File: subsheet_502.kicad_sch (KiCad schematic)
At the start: 26 parts, among them U500 74F374_OCTAL_D-TYPE_EDGE-TRIG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, U501 74F374_OCTAL_D-TYPE_EDGE-TRIG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, U502 DAC0802LCN_PHY, U503 DAC0802LCN_PHY

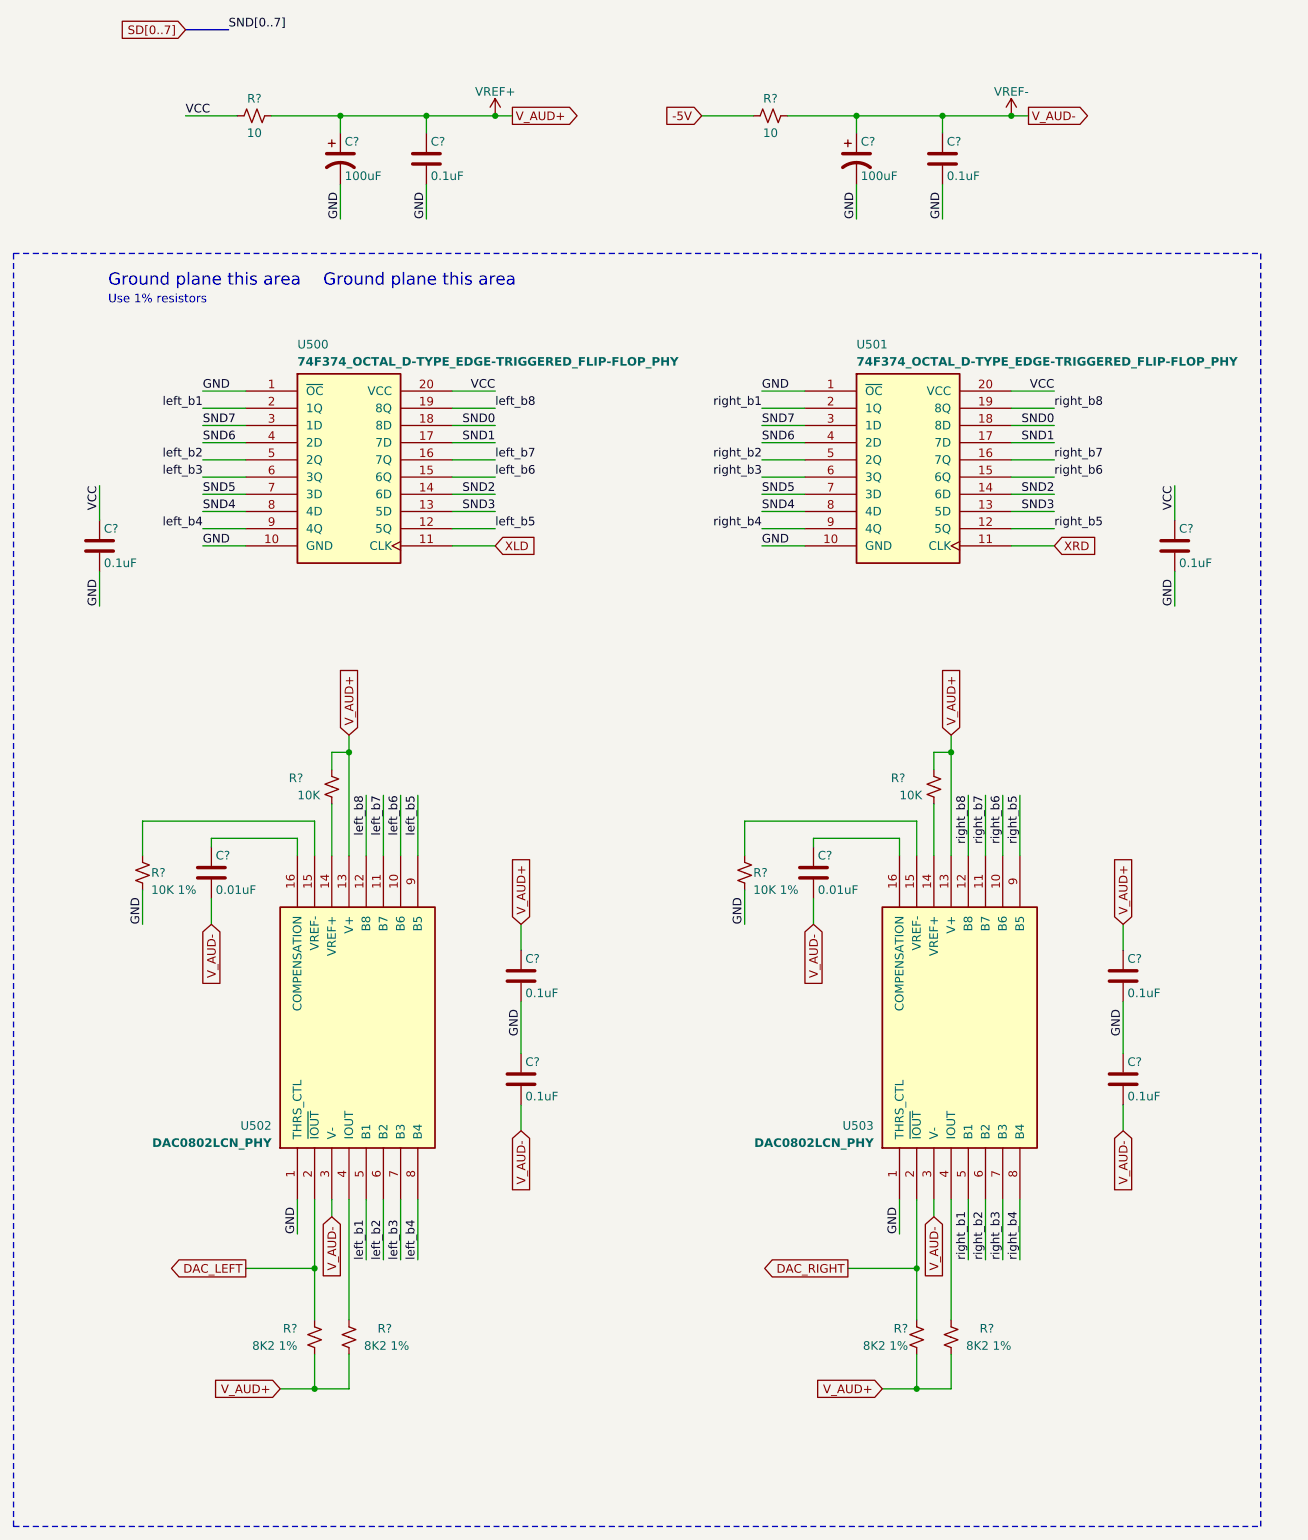
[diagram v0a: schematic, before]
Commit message: Resolves #3 : [schematic] annotate video port with signal name
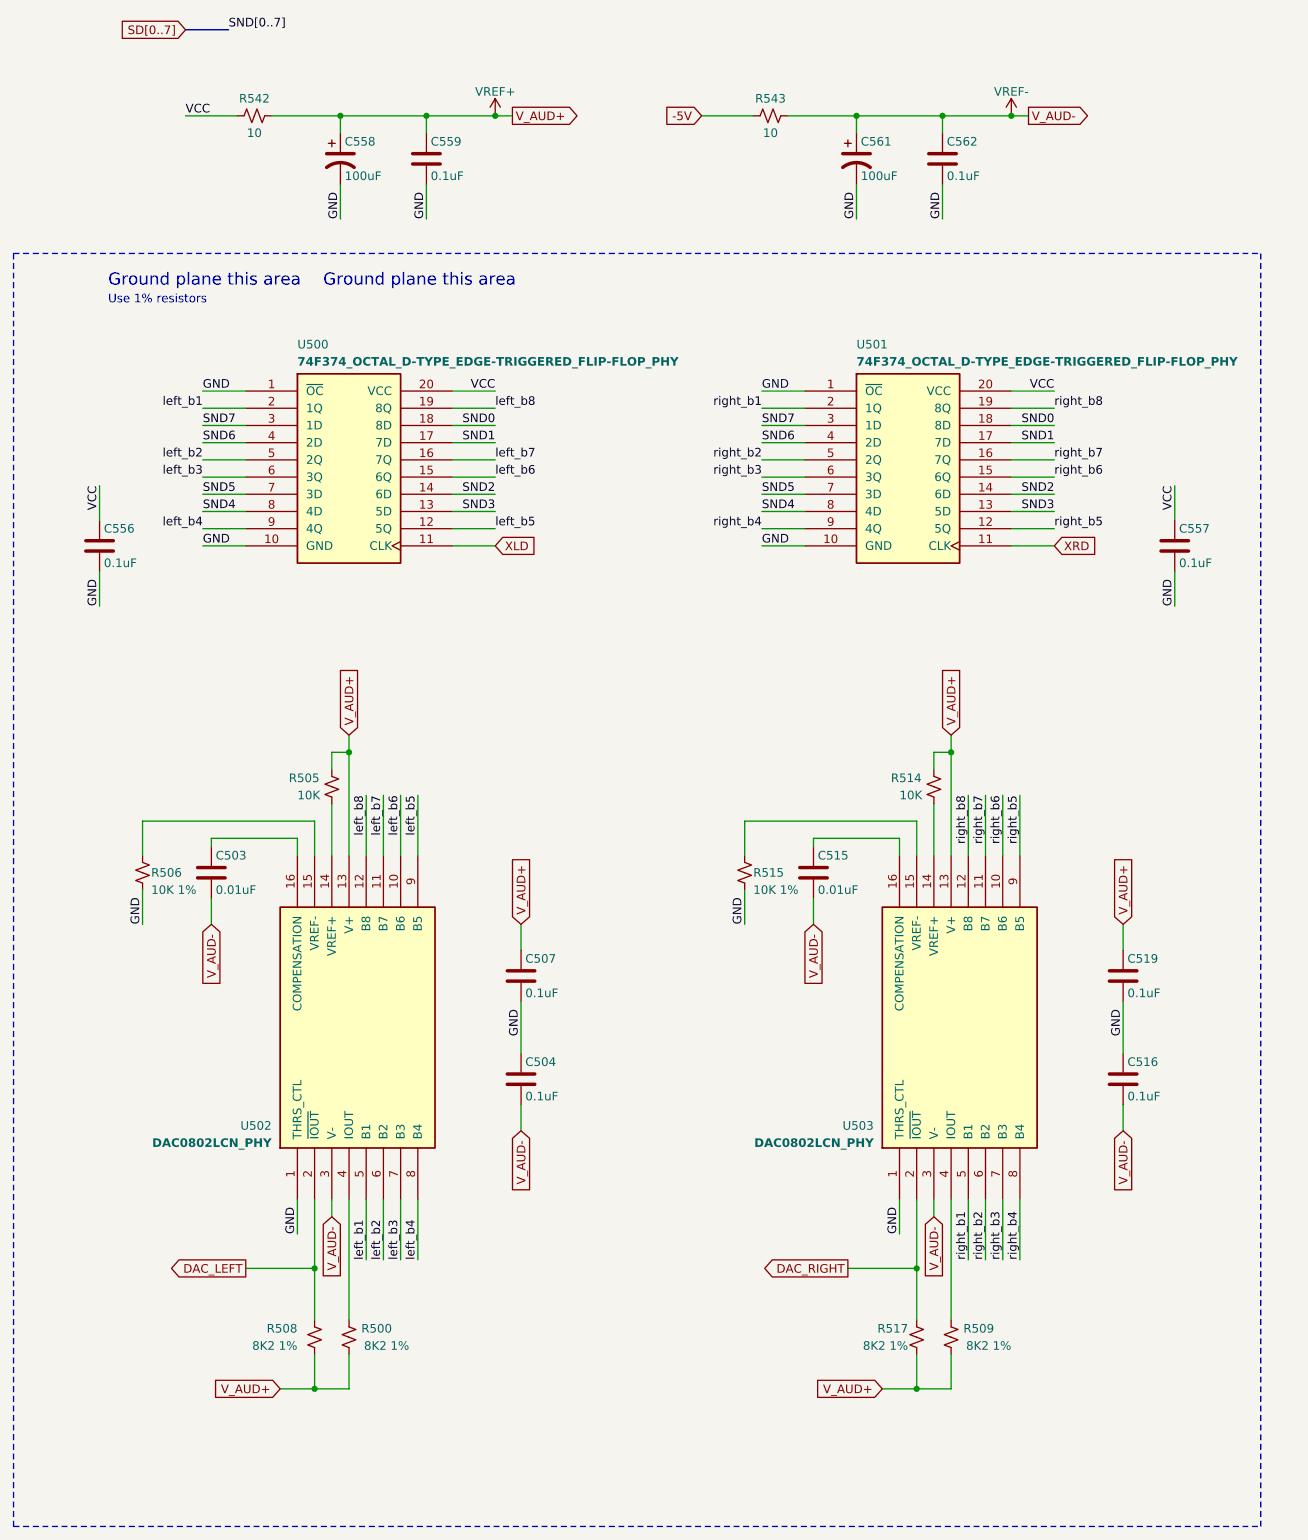
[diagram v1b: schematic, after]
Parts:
- gave numbers to parts that had none: 22
